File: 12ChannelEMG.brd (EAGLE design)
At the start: 54.6 x 196.8 mm, 311 parts

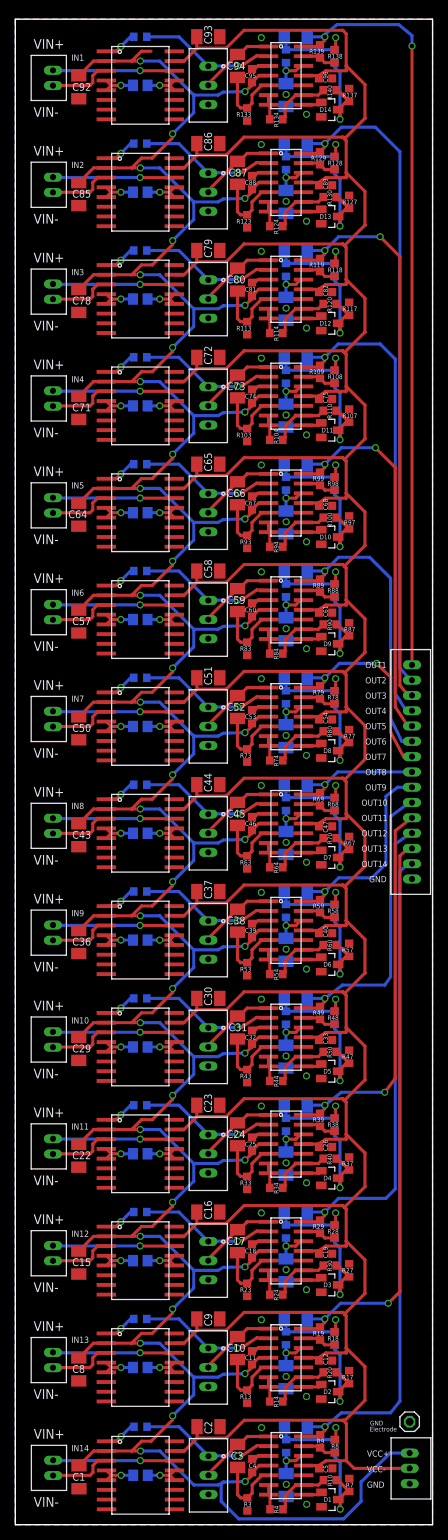
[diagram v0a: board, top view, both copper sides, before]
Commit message: Added Mounting holes in each corner
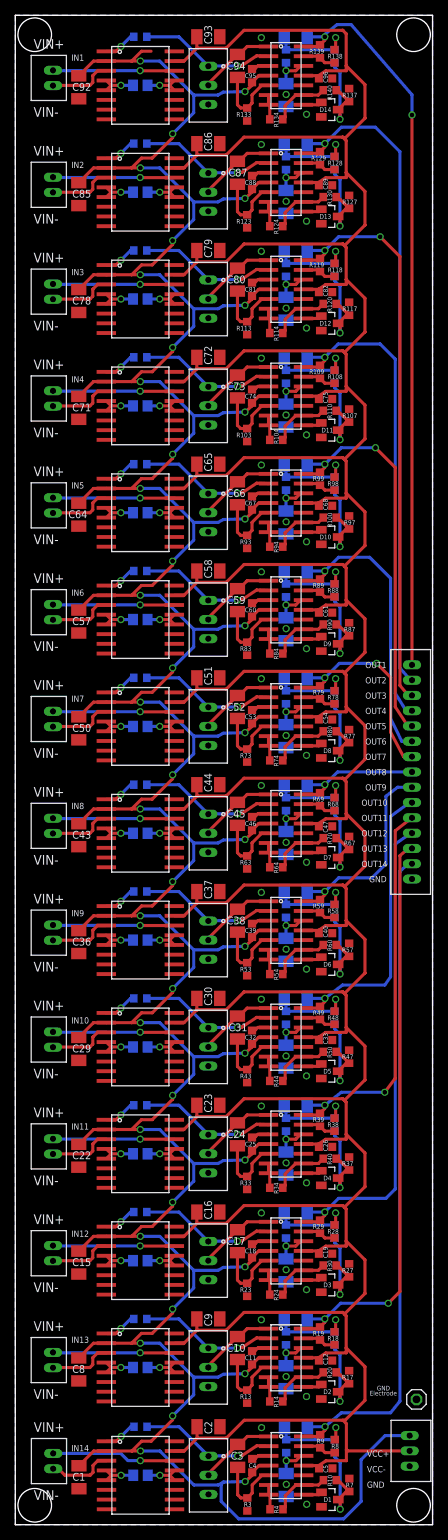
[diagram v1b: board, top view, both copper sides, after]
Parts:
- moved GND 3.05 mm to (52.5, 16.4)
- moved U$57 2.29 mm to (51.6, 9.65)
- moved U$10 0.89 mm to (4.95, 8.32)
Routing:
- net N$222: track 100.9 -> 96.8 mm
- net VCC+: track 615.3 -> 618.0 mm
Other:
- board size 54.6 x 196.8 mm -> 54.6 x 197.4 mm
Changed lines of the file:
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@@
 <setting verticaltext="up"/>
 </settings>
-<grid distance="6" unitdist="mil" unit="mil" style="lines" multiple="1" display="yes" altdistance="0.025" altunitdist="inch" altunit="inch"/>
+<grid distance="5" unitdist="mil" unit="mil" style="lines" multiple="1" display="yes" altdistance="0.025" altunitdist="inch" altunit="inch"/>
 <layers>
 <layer number="1" name="Top" color="4" fill="1" visible="yes" active="yes"/>
@@
 <layer number="43" name="vRestrict" color="2" fill="10" visible="yes" active="yes"/>
 <layer number="44" name="Drills" color="7" fill="1" visible="no" active="yes"/>
-<layer number="45" name="Holes" color="7" fill="1" visible="no" active="yes"/>
+<layer number="45" name="Holes" color="7" fill="1" visible="yes" active="yes"/>
 <layer number="46" name="Milling" color="3" fill="1" visible="no" active="yes"/>
 <layer number="47" name="Measures" color="7" fill="1" visible="no" active="yes"/>
@@
 <plain>
 <wire x1="0" y1="0" x2="54.5592" y2="0" width="0" layer="20"/>
-<wire x1="54.5592" y1="0" x2="54.5592" y2="196.85" width="0" layer="20"/>
-<wire x1="54.5592" y1="196.85" x2="0" y2="196.85" width="0" layer="20"/>
-<wire x1="0" y1="196.85" x2="0" y2="0" width="0" layer="20"/>
+<wire x1="54.5592" y1="0" x2="54.5592" y2="197.358" width="0" layer="20"/>
+<wire x1="54.5592" y1="197.358" x2="0" y2="197.358" width="0" layer="20"/>
+<wire x1="0" y1="197.358" x2="0" y2="0" width="0" layer="20"/>
 <text x="45.974" y="6.858" size="0.8128" layer="25">VCC-</text>
 <text x="45.974" y="8.89" size="0.8128" layer="25">VCC+</text>
@@
 <text x="45.2568" y="88" size="0.8128" layer="25">OUT13</text>
 <text x="45.2568" y="86" size="0.8128" layer="25">OUT14</text>
-<text x="46.3296" y="12.192" size="0.6096" layer="25">Electrode</text>
+<text x="46.3296" y="16.891" size="0.6096" layer="25">Electrode</text>
 <text x="7.3152" y="191.4144" size="0.8128" layer="25">IN1</text>
 <text x="7.3152" y="177.3936" size="0.8128" layer="25">IN2</text>
@@
 <text x="7.3152" y="23.7744" size="0.8128" layer="25">IN13</text>
 <text x="7.3152" y="9.6012" size="0.8128" layer="25">IN14</text>
+<hole x="2.54" y="194.818" drill="4.3942"/>
+<hole x="52.07" y="194.818" drill="4.3942"/>
+<hole x="52.07" y="2.54" drill="4.3942"/>
+<hole x="2.54" y="2.54" drill="4.3942"/>
 </plain>
 <attributes>
@@
 <attribute name="NAME" x="41.453915625" y="5.02791875" size="0.6096" layer="25" rot="R90"/>
 </element>
-<element name="GND" library="pinhead" package="1X01" value="GND" x="51.562" y="13.462" smashed="yes">
-<attribute name="VALUE" x="46.3804" y="12.9794" size="0.6096" layer="25"/>
+<element name="GND" library="pinhead" package="1X01" value="GND" x="52.451" y="16.383" smashed="yes">
+<attribute name="VALUE" x="47.2694" y="17.5514" size="0.6096" layer="25"/>
 </element>
-<element name="U$10" library="12-ChannelEMG" package="2PIN" value="2PIN" x="4.953" y="7.4295" smashed="yes"/>
+<element name="U$10" library="12-ChannelEMG" package="2PIN" value="2PIN" x="4.953" y="8.3185" smashed="yes"/>
 <element name="U$4" library="12-ChannelEMG" package="SOIC167.5MM" value="INA101KU" x="16.3467375" y="20.558346875"/>
 <element name="R11" library="rcl" package="R0805" value="50k" x="16.3467375" y="20.558346875" smashed="yes" rot="MR180">
@@
 </element>
 <element name="U$56" library="12-ChannelEMG" package="2PIN" value="2PIN" x="4.9276" y="189.1665"/>
-<element name="U$57" library="12-ChannelEMG" package="3PIN" value="3PIN" x="51.562" y="7.366" rot="R180"/>
+<element name="U$57" library="12-ChannelEMG" package="3PIN" value="3PIN" x="51.562" y="9.652" rot="R180"/>
 <element name="U$58" library="12-ChannelEMG" package="15PIN" value="15PIN" x="51.8668" y="98.425"/>
 </elements>
@@
 <wire x1="17.907" y1="178.689" x2="20.574" y2="181.356" width="0.4064" layer="1"/>
 <contactref element="U$57" pad="3"/>
-<wire x1="45.212" y1="5.588" x2="45.212" y2="3.048" width="0.4064" layer="16"/>
 <wire x1="45.212" y1="3.048" x2="42.926" y2="0.762" width="0.4064" layer="16"/>
 <wire x1="42.926" y1="0.762" x2="29.21" y2="0.762" width="0.4064" layer="16"/>
@@
 <wire x1="26.924" y1="3.048" x2="26.924" y2="5.278596875" width="0.4064" layer="16"/>
 <wire x1="26.924" y1="5.278596875" x2="27.220109375" y2="5.57470625" width="0.4064" layer="16"/>
-<wire x1="51.562" y1="9.366" x2="48.99" y2="9.366" width="0.4064" layer="16"/>
-<wire x1="48.99" y1="9.366" x2="45.212" y2="5.588" width="0.4064" layer="16"/>
+<wire x1="51.562" y1="11.652" x2="48.355" y2="11.652" width="0.4064" layer="16"/>
+<wire x1="48.355" y1="11.652" x2="45.212" y2="8.509" width="0.4064" layer="16"/>
+<wire x1="45.212" y1="8.509" x2="45.212" y2="3.048" width="0.4064" layer="16"/>
 </signal>
 <signal name="N$2">
@@
 <wire x1="22.0871375" y1="9.636346875" x2="20.8171375" y2="9.636346875" width="0.4064" layer="1"/>
 <wire x1="40.616765625" y1="8.356559375" x2="43.289565625" y2="8.370540625" width="0.4064" layer="1"/>
-<wire x1="43.289565625" y1="8.370540625" x2="43.289565625" y2="13.212025" width="0.4064" layer="1"/>
+<wire x1="43.289565625" y1="8.370540625" x2="43.289565625" y2="9.779" width="0.4064" layer="1"/>
+<wire x1="43.289565625" y1="9.779" x2="43.289565625" y2="13.212025" width="0.4064" layer="1"/>
 <wire x1="43.289565625" y1="13.212025" x2="42.8407" y2="13.660890625" width="0.4064" layer="1"/>
 <wire x1="42.8407" y1="13.660890625" x2="29.933509375" y2="13.660890625" width="0.4064" layer="1"/>
@@
 <wire x1="45.719996875" y1="183.896" x2="43.03359375" y2="181.209596875" width="0.4064" layer="1"/>
 <contactref element="U$57" pad="2"/>
-<wire x1="51.562" y1="7.366" x2="44.29410625" y2="7.366" width="0.4064" layer="1"/>
-<wire x1="44.29410625" y1="7.366" x2="43.289565625" y2="8.370540625" width="0.4064" layer="1"/>
+<wire x1="51.562" y1="9.652" x2="43.49623125" y2="9.652" width="0.4064" layer="1"/>
+<wire x1="43.49623125" y1="9.652" x2="43.360234375" y2="9.70833125" width="0.4064" layer="1" curve="-45"/>
+<wire x1="43.360234375" y1="9.70833125" x2="43.289565625" y2="9.779" width="0.4064" layer="1"/>
 </signal>
 <signal name="GND">
@@
 <vertex x="0" y="0"/>
 <vertex x="54.5592" y="0"/>
-<vertex x="54.5592" y="196.85"/>
-<vertex x="0" y="196.85"/>
+<vertex x="54.5592" y="197.358"/>
+<vertex x="0" y="197.358"/>
 </polygon>
 <polygon width="0.4064" layer="16">
 <vertex x="0" y="0"/>
 <vertex x="54.5592" y="0"/>
-<vertex x="54.5592" y="196.85"/>
-<vertex x="0" y="196.85"/>
+<vertex x="54.5592" y="197.358"/>
+<vertex x="0" y="197.358"/>
 </polygon>
 <via x="32.1945" y="12.7" extent="1-16" drill="0.6"/>
@@
 <wire x1="10.16" y1="7.747" x2="10.16" y2="6.8326" width="0.4064" layer="1"/>
 <wire x1="10.16" y1="6.8326" x2="9.779" y2="6.4516" width="0.4064" layer="1"/>
-<wire x1="9.779" y1="6.4516" x2="4.9751" y2="6.4516" width="0.4064" layer="1"/>
-<wire x1="4.9751" y1="6.4516" x2="4.953" y2="6.4295" width="0.4064" layer="1"/>
+<wire x1="4.953" y1="7.3185" x2="5.6355" y2="7.3185" width="0.4064" layer="1"/>
+<wire x1="5.6355" y1="7.3185" x2="6.477" y2="6.477" width="0.4064" layer="1"/>
+<wire x1="6.477" y1="6.477" x2="9.7536" y2="6.477" width="0.4064" layer="1"/>
+<wire x1="9.7536" y1="6.477" x2="9.779" y2="6.4516" width="0.4064" layer="1"/>
 </signal>
 <signal name="N$5">
@@
 <wire x1="16.525653125" y1="8.366346875" x2="16.35125" y2="8.382" width="0.4064" layer="1"/>
 <via x="16.35125" y="8.382" extent="1-16" drill="0.6"/>
-<wire x1="16.35125" y1="8.382" x2="4.953" y2="8.382" width="0.4064" layer="16"/>
 <contactref element="U$10" pad="1"/>
-<wire x1="4.953" y1="8.382" x2="4.953" y2="8.4295" width="0.4064" layer="16"/>
+<wire x1="4.953" y1="9.3185" x2="13.7955" y2="9.3185" width="0.4064" layer="16"/>
+<wire x1="13.7955" y1="9.3185" x2="14.732" y2="8.382" width="0.4064" layer="16"/>
+<wire x1="14.732" y1="8.382" x2="16.35125" y2="8.382" width="0.4064" layer="16"/>
 </signal>
 <signal name="N$13">
@@
 <wire x1="39.6267375" y1="193.278346875" x2="39.8417375" y2="193.493346875" width="0.4064" layer="1"/>
 <contactref element="U$58" pad="1"/>
-<wire x1="51.8668" y1="112.425" x2="51.8668" y2="193.3448" width="0.4064" layer="1"/>
+<wire x1="51.8668" y1="112.425" x2="51.8668" y2="184.3278" width="0.4064" layer="1"/>
 <wire x1="40.492390625" y1="194.564" x2="40.4767375" y2="194.548346875" width="0.4064" layer="16"/>
 <wire x1="40.4767375" y1="194.548346875" x2="40.4767375" y2="194.8579375" width="0.4064" layer="16"/>
 <wire x1="40.4767375" y1="194.8579375" x2="42.0624" y2="196.1388" width="0.4064" layer="16"/>
-<via x="51.8668" y="193.3448" extent="1-16" drill="0.6"/>
-<wire x1="51.8668" y1="193.3448" x2="51.8668" y2="194.7164" width="0.4064" layer="16"/>
-<wire x1="51.8668" y1="194.7164" x2="50.1396" y2="196.1388" width="0.4064" layer="16"/>
-<wire x1="50.1396" y1="196.1388" x2="42.0624" y2="196.1388" width="0.4064" layer="16"/>
+<via x="51.8668" y="184.3278" extent="1-16" drill="0.6"/>
+<wire x1="51.8668" y1="184.3278" x2="51.8668" y2="186.9694" width="0.4064" layer="16"/>
+<wire x1="51.8668" y1="186.9694" x2="43.9166" y2="196.1388" width="0.4064" layer="16"/>
+<wire x1="43.9166" y1="196.1388" x2="42.0624" y2="196.1388" width="0.4064" layer="16"/>
 </signal>
 <signal name="N$223">
@@
 <wire x1="16.500253125" y1="190.103346875" x2="16.32585" y2="190.119" width="0.4064" layer="1"/>
 <via x="16.32585" y="190.119" extent="1-16" drill="0.6"/>
-<wire x1="16.32585" y1="190.119" x2="4.9276" y2="190.119" width="0.4064" layer="16"/>
 <contactref element="U$56" pad="1"/>
 <wire x1="4.9276" y1="190.119" x2="4.9276" y2="190.1665" width="0.4064" layer="16"/>
+<wire x1="16.32585" y1="190.119" x2="4.9276" y2="190.119" width="0.4064" layer="16"/>
 </signal>
 </signals>
-<errors>
-</errors>
 </board>
 </drawing>

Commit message: Added center mounting holes
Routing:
- net N$110: track 18.0 -> 20.7 mm
- net VCC-: track 676.5 -> 675.4 mm
- net N$46: track 64.1 -> 64.6 mm
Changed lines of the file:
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@@
 <hole x="52.07" y="2.54" drill="4.3942"/>
 <hole x="2.54" y="2.54" drill="4.3942"/>
+<hole x="8.3312" y="98.044" drill="4.3942"/>
+<hole x="46.228" y="98.044" drill="4.3942"/>
 </plain>
 <attributes>
@@
 <wire x1="43.264165625" y1="92.317540625" x2="43.264165625" y2="92.964" width="0.4064" layer="1"/>
 <wire x1="43.264165625" y1="92.964" x2="43.264165625" y2="97.159025" width="0.4064" layer="1"/>
-<wire x1="43.264165625" y1="97.159025" x2="43.03359375" y2="97.389596875" width="0.4064" layer="1"/>
-<wire x1="43.03359375" y1="97.389596875" x2="42.8153" y2="97.607890625" width="0.4064" layer="1"/>
+<wire x1="43.264165625" y1="97.159025" x2="42.8153" y2="97.607890625" width="0.4064" layer="1"/>
 <wire x1="42.8153" y1="97.607890625" x2="29.908109375" y2="97.607890625" width="0.4064" layer="1"/>
 <wire x1="29.908109375" y1="97.607890625" x2="27.58504375" y2="95.284825" width="0.4064" layer="1"/>
@@
 <wire x1="22.0617375" y1="107.553346875" x2="20.7917375" y2="107.553346875" width="0.4064" layer="1"/>
 <wire x1="40.591365625" y1="106.273559375" x2="43.264165625" y2="106.287540625" width="0.4064" layer="1"/>
-<wire x1="43.264165625" y1="106.287540625" x2="43.264165625" y2="106.934" width="0.4064" layer="1"/>
-<wire x1="43.264165625" y1="106.934" x2="43.264165625" y2="111.129025" width="0.4064" layer="1"/>
+<wire x1="43.264165625" y1="106.287540625" x2="43.264165625" y2="111.129025" width="0.4064" layer="1"/>
 <wire x1="43.264165625" y1="111.129025" x2="43.03359375" y2="111.359596875" width="0.4064" layer="1"/>
 <wire x1="43.03359375" y1="111.359596875" x2="42.8153" y2="111.577890625" width="0.4064" layer="1"/>
@@
 <wire x1="39.6422375" y1="105.648346875" x2="40.591365625" y2="106.273559375" width="0.4064" layer="1"/>
 <wire x1="42.8153" y1="111.577890625" x2="42.845490625" y2="111.577890625" width="0.4064" layer="1"/>
-<wire x1="45.72" y1="100.076" x2="45.72" y2="104.478165625" width="0.4064" layer="1"/>
-<wire x1="45.72" y1="104.478165625" x2="43.264165625" y2="106.934" width="0.4064" layer="1"/>
-<wire x1="45.72" y1="100.076" x2="45.719996875" y2="100.076" width="0.4064" layer="1"/>
-<wire x1="45.719996875" y1="100.076" x2="43.03359375" y2="97.389596875" width="0.4064" layer="1"/>
 <contactref element="U$33" pad="15"/>
 <contactref element="C58" pad="1"/>
@@
 <wire x1="43.49623125" y1="9.652" x2="43.360234375" y2="9.70833125" width="0.4064" layer="1" curve="-45"/>
 <wire x1="43.360234375" y1="9.70833125" x2="43.289565625" y2="9.779" width="0.4064" layer="1"/>
+<wire x1="42.8153" y1="97.607890625" x2="42.8153" y2="98.1873" width="0.4064" layer="1"/>
+<wire x1="42.8153" y1="98.1873" x2="45.593" y2="101.854" width="0.4064" layer="1"/>
+<wire x1="45.593" y1="101.854" x2="45.593" y2="103.95870625" width="0.4064" layer="1"/>
+<wire x1="45.593" y1="103.95870625" x2="43.264165625" y2="106.287540625" width="0.4064" layer="1"/>
 </signal>
 <signal name="GND">
@@
 <contactref element="U$57" pad="1"/>
 <contactref element="U$58" pad="15"/>
+<wire x1="41.7467375" y1="95.068346875" x2="41.7467375" y2="95.0867375" width="0.4064" layer="1"/>
+<wire x1="41.7467375" y1="95.0867375" x2="41.783" y2="95.123" width="0.4064" layer="1"/>
 </signal>
 <signal name="N$6">
@@
 <wire x1="39.6267375" y1="39.608346875" x2="39.8417375" y2="39.823346875" width="0.4064" layer="1"/>
 <contactref element="U$58" pad="12"/>
-<wire x1="49.6824" y1="89.0016" x2="49.6824" y2="43.8912" width="0.4064" layer="16"/>
+<wire x1="49.6824" y1="89.6874" x2="49.6824" y2="43.8912" width="0.4064" layer="16"/>
 <wire x1="40.492390625" y1="40.894" x2="40.4767375" y2="40.878346875" width="0.4064" layer="16"/>
 <wire x1="42.270390625" y1="42.672" x2="40.4767375" y2="40.878346875" width="0.4064" layer="16"/>
-<wire x1="51.8668" y1="90.424" x2="51.7144" y2="90.424" width="0.4064" layer="16"/>
-<wire x1="51.7144" y1="90.424" x2="49.6824" y2="89.0016" width="0.4064" layer="16"/>
 <wire x1="49.6824" y1="43.8912" x2="48.4632" y2="42.672" width="0.4064" layer="16"/>
 <wire x1="48.4632" y1="42.672" x2="42.270390625" y2="42.672" width="0.4064" layer="16"/>
-<wire x1="51.8668" y1="90.424" x2="51.8668" y2="90.425" width="0" layer="19" extent="16-16"/>
+<wire x1="51.8658" y1="90.424" x2="51.8668" y2="90.425" width="0.4064" layer="16"/>
+<wire x1="49.6824" y1="89.6874" x2="50.419" y2="90.424" width="0.4064" layer="16"/>
+<wire x1="50.419" y1="90.424" x2="51.8658" y2="90.424" width="0.4064" layer="16"/>
 </signal>
 <signal name="N$47">
@@
 <contactref element="U$58" pad="9"/>
 <wire x1="51.8668" y1="96.425" x2="49.9938" y2="96.425" width="0.4064" layer="16"/>
-<wire x1="49.9938" y1="96.425" x2="48.4632" y2="95.25" width="0.4064" layer="16"/>
-<wire x1="48.4632" y1="95.25" x2="48.4632" y2="86.36" width="0.4064" layer="16"/>
+<wire x1="49.9938" y1="96.425" x2="48.4632" y2="94.488" width="0.4064" layer="16"/>
+<wire x1="48.4632" y1="94.488" x2="48.4632" y2="86.36" width="0.4064" layer="16"/>
 <wire x1="42.270390625" y1="84.582" x2="40.4767375" y2="82.788346875" width="0.4064" layer="16"/>
 <wire x1="48.4632" y1="86.36" x2="48.4124" y2="86.36" width="0.4064" layer="16"/>
@@
 <contactref element="U$58" pad="8"/>
 <wire x1="40.492390625" y1="96.774" x2="40.4767375" y2="96.758346875" width="0.4064" layer="16"/>
-<wire x1="51.8668" y1="98.425" x2="42.143390625" y2="98.425" width="0.4064" layer="16"/>
-<wire x1="42.143390625" y1="98.425" x2="40.4767375" y2="96.758346875" width="0.4064" layer="16"/>
+<wire x1="40.4767375" y1="96.758346875" x2="40.4767375" y2="97.1187375" width="0.4064" layer="16"/>
+<wire x1="40.4767375" y1="97.1187375" x2="41.021" y2="97.79" width="0.4064" layer="16"/>
+<wire x1="41.021" y1="97.79" x2="42.799" y2="97.79" width="0.4064" layer="16"/>
+<wire x1="42.799" y1="97.79" x2="43.942" y2="95.885" width="0.4064" layer="16"/>
+<wire x1="43.942" y1="95.885" x2="44.45" y2="95.25" width="0.4064" layer="16"/>
+<wire x1="44.45" y1="95.25" x2="47.752" y2="95.25" width="0.4064" layer="16"/>
+<wire x1="47.752" y1="95.25" x2="50.419" y2="98.044" width="0.4064" layer="16"/>
+<wire x1="50.419" y1="98.044" x2="51.4858" y2="98.044" width="0.4064" layer="16"/>
+<wire x1="51.4858" y1="98.044" x2="51.8668" y2="98.425" width="0.4064" layer="16"/>
 </signal>
 <signal name="N$111">
@@
 <wire x1="41.7467375" y1="107.338346875" x2="41.7467375" y2="106.7543625" width="0.4064" layer="16"/>
 <wire x1="41.7467375" y1="106.7543625" x2="42.4561" y2="106.045" width="0.4064" layer="16"/>
-<wire x1="42.4561" y1="106.045" x2="42.4561" y2="99.949" width="0.4064" layer="16"/>
-<via x="42.4561" y="99.949" extent="1-16" drill="0.6"/>
-<wire x1="42.4561" y1="99.949" x2="42.4561" y2="100.958984375" width="0.4064" layer="1"/>
+<wire x1="42.4561" y1="106.045" x2="42.4561" y2="100.076" width="0.4064" layer="16"/>
+<via x="42.4561" y="100.076" extent="1-16" drill="0.6"/>
+<wire x1="42.4561" y1="100.076" x2="42.4561" y2="100.958984375" width="0.4064" layer="1"/>
 <wire x1="42.4561" y1="100.958984375" x2="42.2117375" y2="101.203346875" width="0.4064" layer="1"/>
 </signal>
@@
 </signal>
 </signals>
+<errors>
+</errors>
 </board>
 </drawing>
